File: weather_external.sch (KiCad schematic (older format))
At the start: 15 parts, among them J1 Conn_01x02_Male, J2 Conn_01x02_Male, SW1 SW_Push

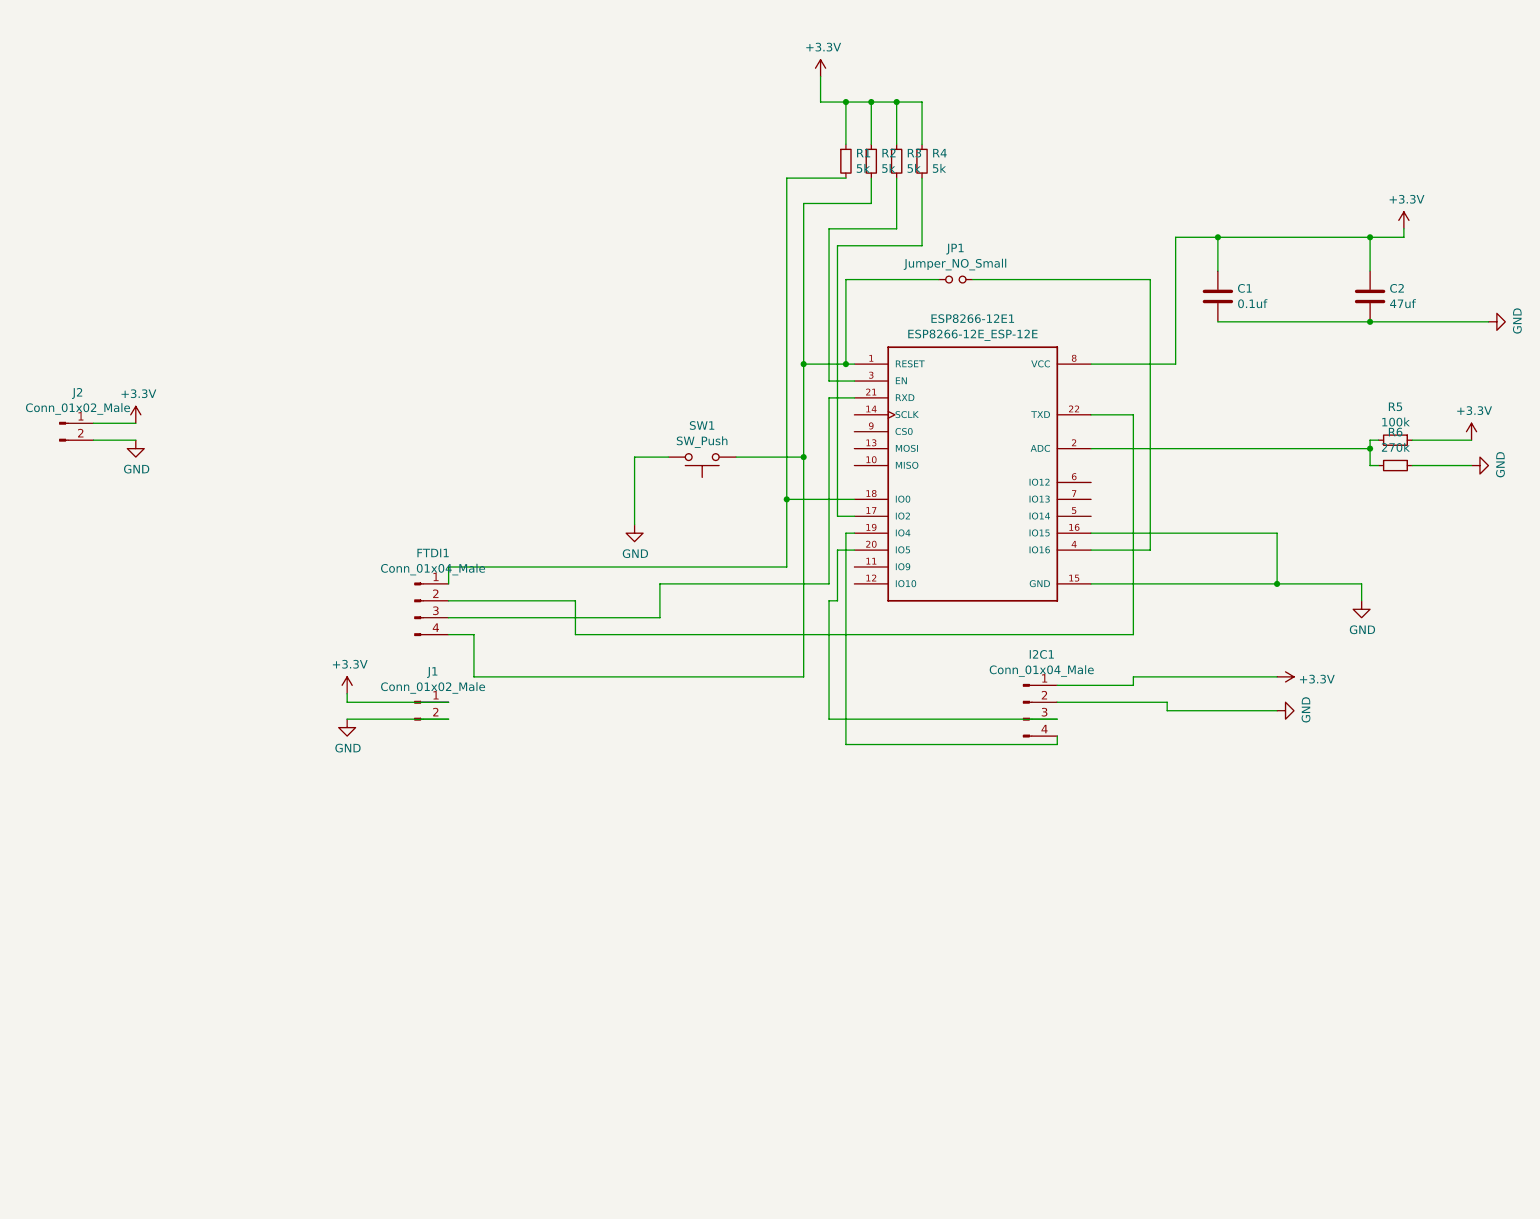
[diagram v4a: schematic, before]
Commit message: No 555 print version
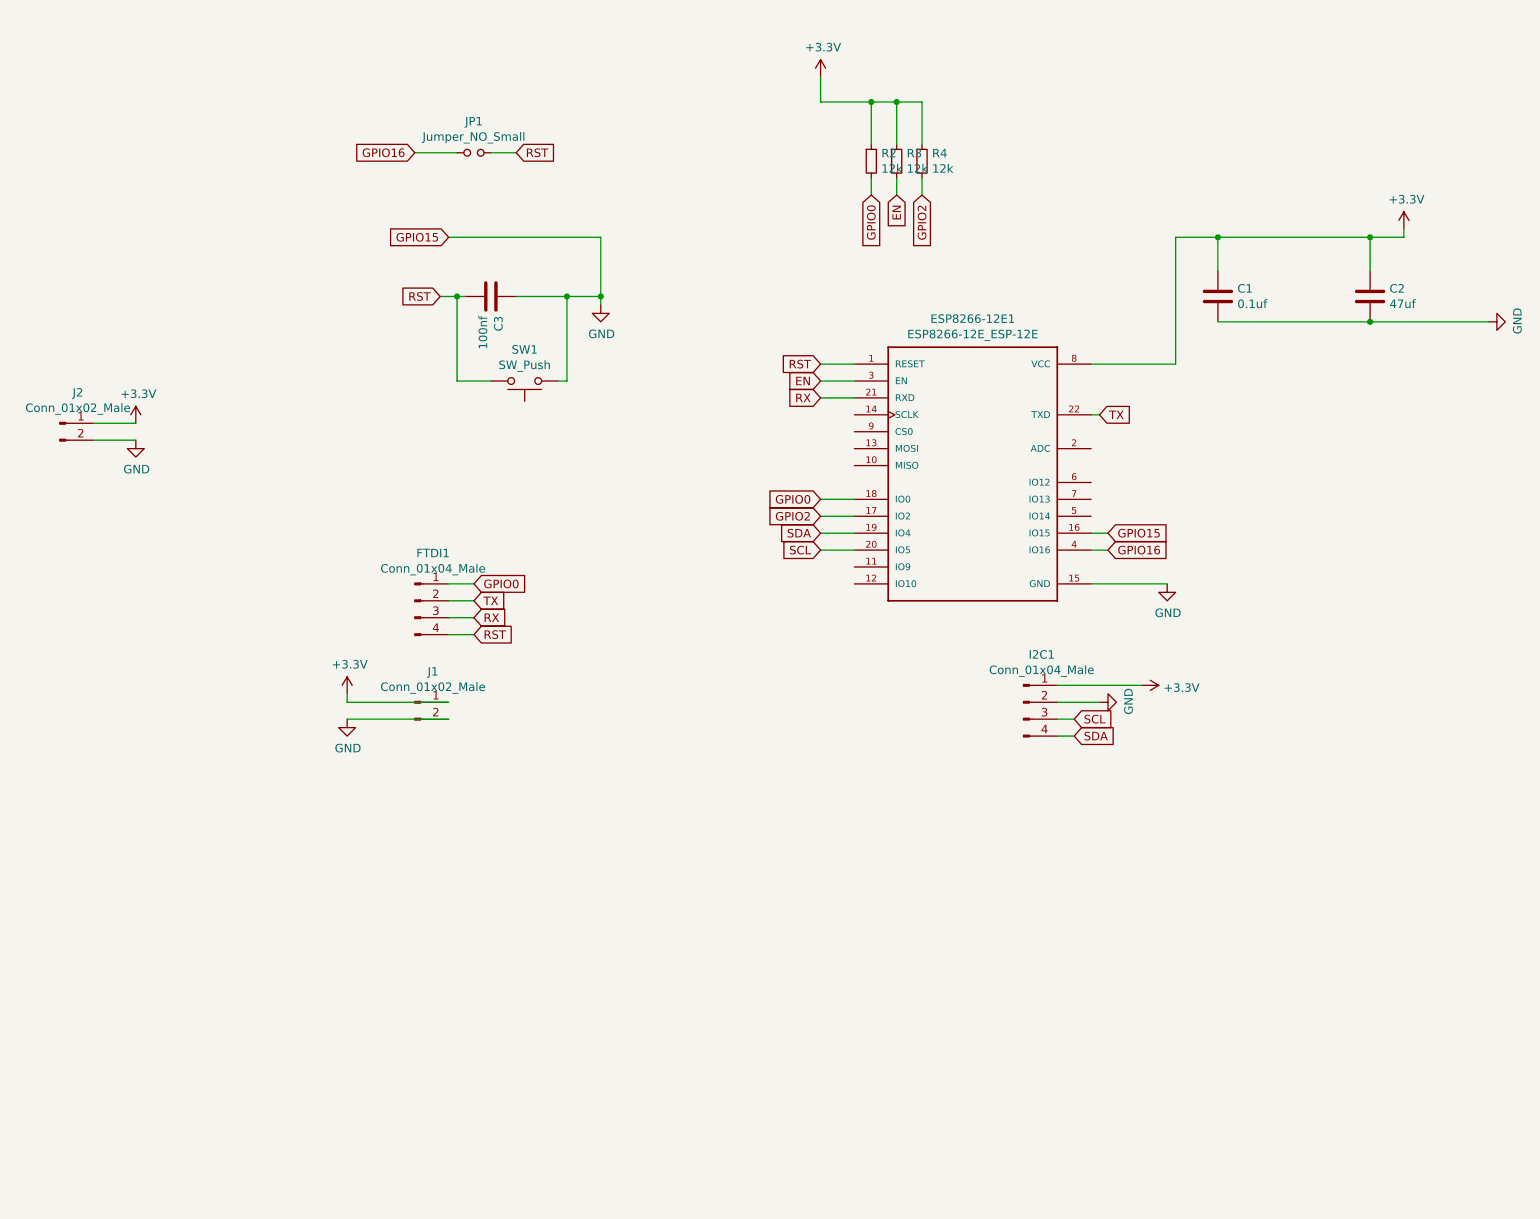
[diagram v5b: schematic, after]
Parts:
- removed R1: 5k, Resistor_THT:R_Axial_DIN0207_L6.3mm_D2.5mm_P7.62mm_Horizontal, symbol Device:R_Small
- removed R5: 100k, Resistor_THT:R_Axial_DIN0207_L6.3mm_D2.5mm_P7.62mm_Horizontal, symbol Device:R_Small
- removed R6: 270k, Resistor_THT:R_Axial_DIN0207_L6.3mm_D2.5mm_P7.62mm_Horizontal, symbol Device:R_Small
- added C3: 100nf, Capacitor_THT:C_Disc_D3.0mm_W1.6mm_P2.50mm, symbol Device:C
- R2, R3, R4: value 5k -> 12k; footprint Resistor_THT:R_Axial_DIN0207_L6.3mm_D2.5mm_P7.62mm_Horizontal -> Resistor_SMD:R_1206_3216Metric_Pad1.42x1.75mm_HandSolder
- SW1: footprint Button_Switch_THT:SW_PUSH_6mm -> Button_Switch_SMD:SW_SPST_CK_RS282G05A3
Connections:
- net GND: now also SW1.1, C3.1; no longer SW1.2
- net GPIO0: now reaches ESP8266-12E1.18 (IO0), FTDI1.1 (Pin_1)
- net GPIO0: now also R2.2
- net TX: now reaches ESP8266-12E1.22 (TXD), FTDI1.2 (Pin_2)
- net RX: now reaches ESP8266-12E1.21 (RXD), FTDI1.3 (Pin_3)
- net GPIO2: now reaches ESP8266-12E1.17 (IO2), R4.2
- net SDA: now reaches ESP8266-12E1.19 (IO4), I2C1.4 (Pin_4)
- net SCL: now reaches ESP8266-12E1.20 (IO5), I2C1.3 (Pin_3)
- net EN: now reaches ESP8266-12E1.3 (EN), R3.2
- net GPIO16: now reaches ESP8266-12E1.4 (IO16)
- net GPIO16: now also JP1.1; no longer JP1.2
- new net RST: C3.2, ESP8266-12E1.1 (RESET), FTDI1.4 (Pin_4), JP1.2, SW1.2
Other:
- moved on the sheet: JP1, SW1

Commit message: JLCPCB version 1.3
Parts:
- JP1: footprint Connector_PinHeader_2.54mm:PinHeader_1x02_P2.54mm_Vertical -> Jumper:SolderJumper-2_P1.3mm_Open_Pad1.0x1.5mm
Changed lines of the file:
@@
 Title ""
 Date ""
-Rev ""
+Rev "1.3 "
 Comp ""
 Comment1 ""
 Comment2 ""
 Comment3 ""
-Comment4 ""
+Comment4 "Jareas"
 $EndDescr
 $Comp
@@
 L power:GND #PWR0110
 U 1 1 5FB0BB1F
-P 7900 4000
-F 0 "#PWR0110" H 7900 3750 50  0001 C CNN
-F 1 "GND" H 7905 3827 50  0000 C CNN
-F 2 "" H 7900 4000 50  0001 C CNN
-F 3 "" H 7900 4000 50  0001 C CNN
-	1    7900 4000
-	1    0    0    -1
+P 7500 4000
+F 0 "#PWR0110" H 7500 3750 50  0001 C CNN
+F 1 "GND" H 7505 3827 50  0000 C CNN
+F 2 "" H 7500 4000 50  0001 C CNN
+F 3 "" H 7500 4000 50  0001 C CNN
+	1    7500 4000
+	0    -1   -1   0
 $EndComp
 $Comp
@@
 F 0 "JP1" H 3800 1635 50  0000 C CNN
 F 1 "Jumper_NO_Small" H 3800 1544 50  0000 C CNN
-F 2 "Connector_PinHeader_2.54mm:PinHeader_1x02_P2.54mm_Vertical" H 3800 1450 50  0001 C CNN
+F 2 "Jumper:SolderJumper-2_P1.3mm_Open_Pad1.0x1.5mm" H 3800 1450 50  0001 C CNN
 F 3 "~" H 3800 1450 50  0001 C CNN
 	1    3800 1450
@@
 Text GLabel 3650 1950 0    50   Input ~ 0
 GPIO15
-Wire Wire Line
-	3650 1950 4550 1950
-Wire Wire Line
-	4550 1950 4550 2300
-Connection ~ 4550 2300
 Text GLabel 7550 3700 2    50   Input ~ 0
 GPIO15
-Wire Wire Line
-	7450 4000 7900 4000
 Text GLabel 3450 1450 0    50   Input ~ 0
 GPIO16
@@
 Wire Wire Line
 	7250 4700 7500 4700
+Wire Wire Line
+	3650 1950 4350 1950
+Wire Wire Line
+	4350 1950 4350 2300
+Wire Wire Line
+	7450 4000 7500 4000
 $EndSCHEMATC

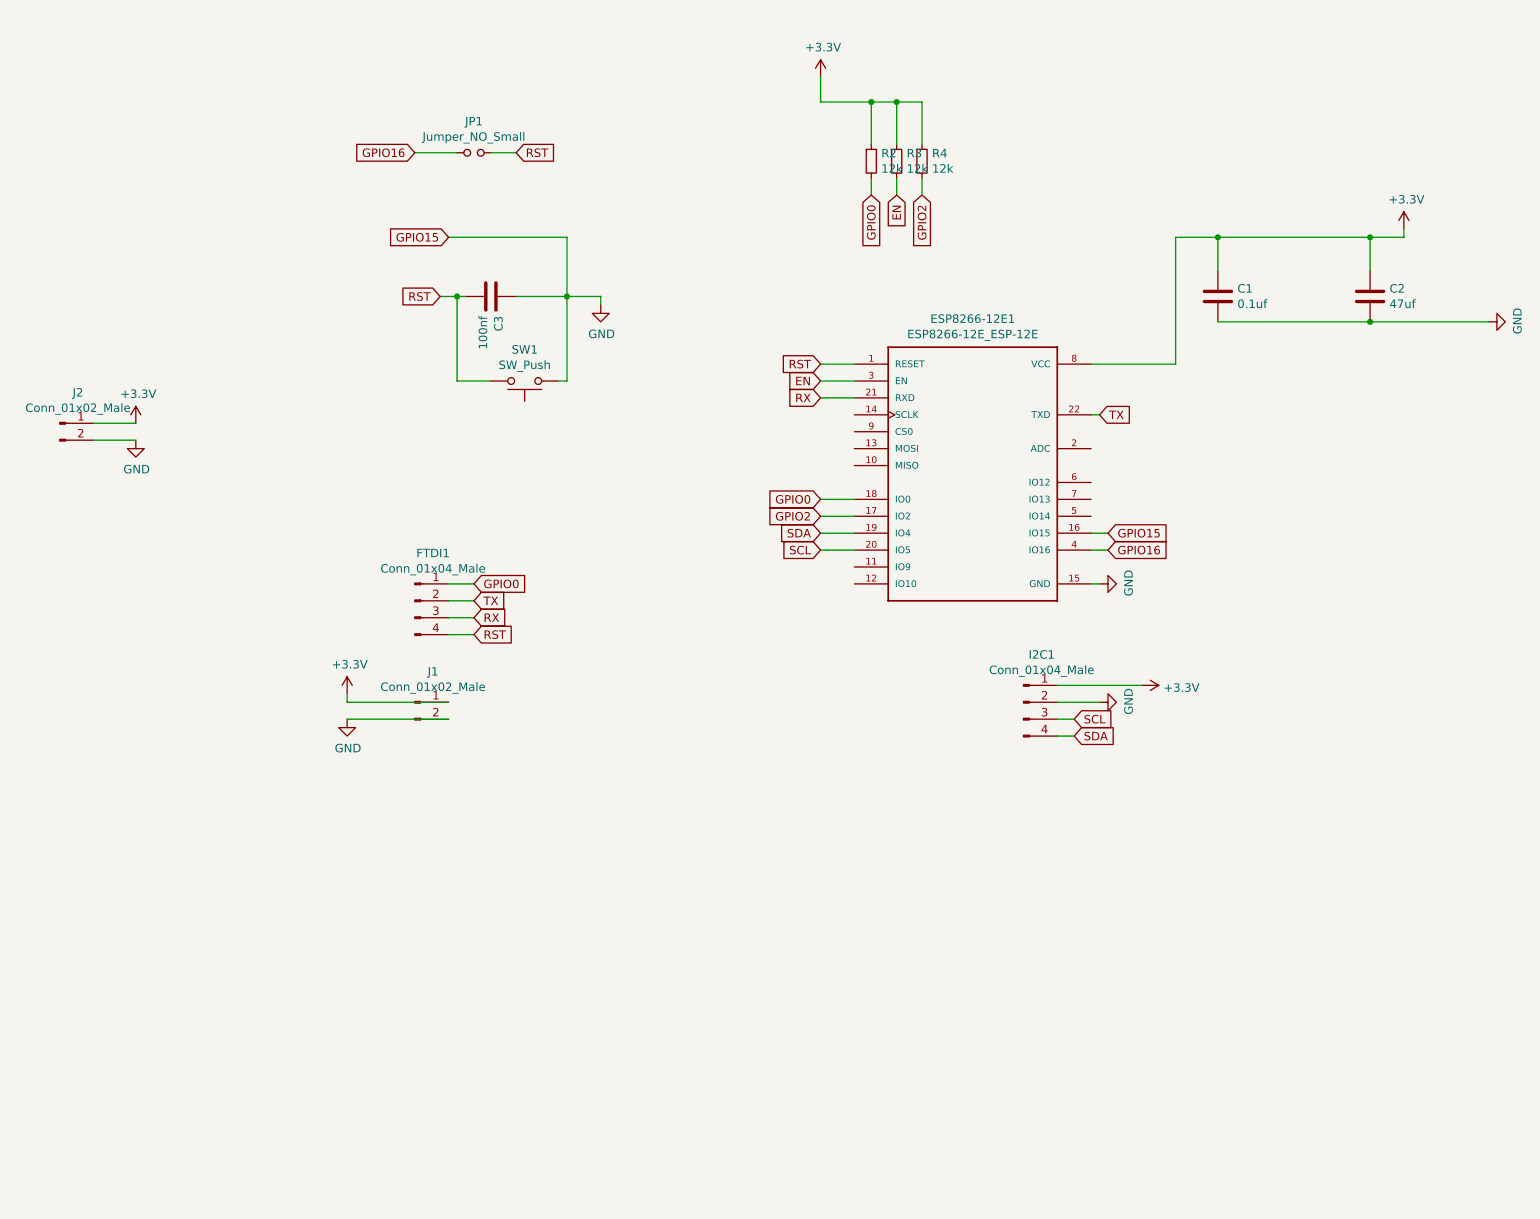
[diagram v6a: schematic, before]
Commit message: - Adding charger module TP4056 - add usb
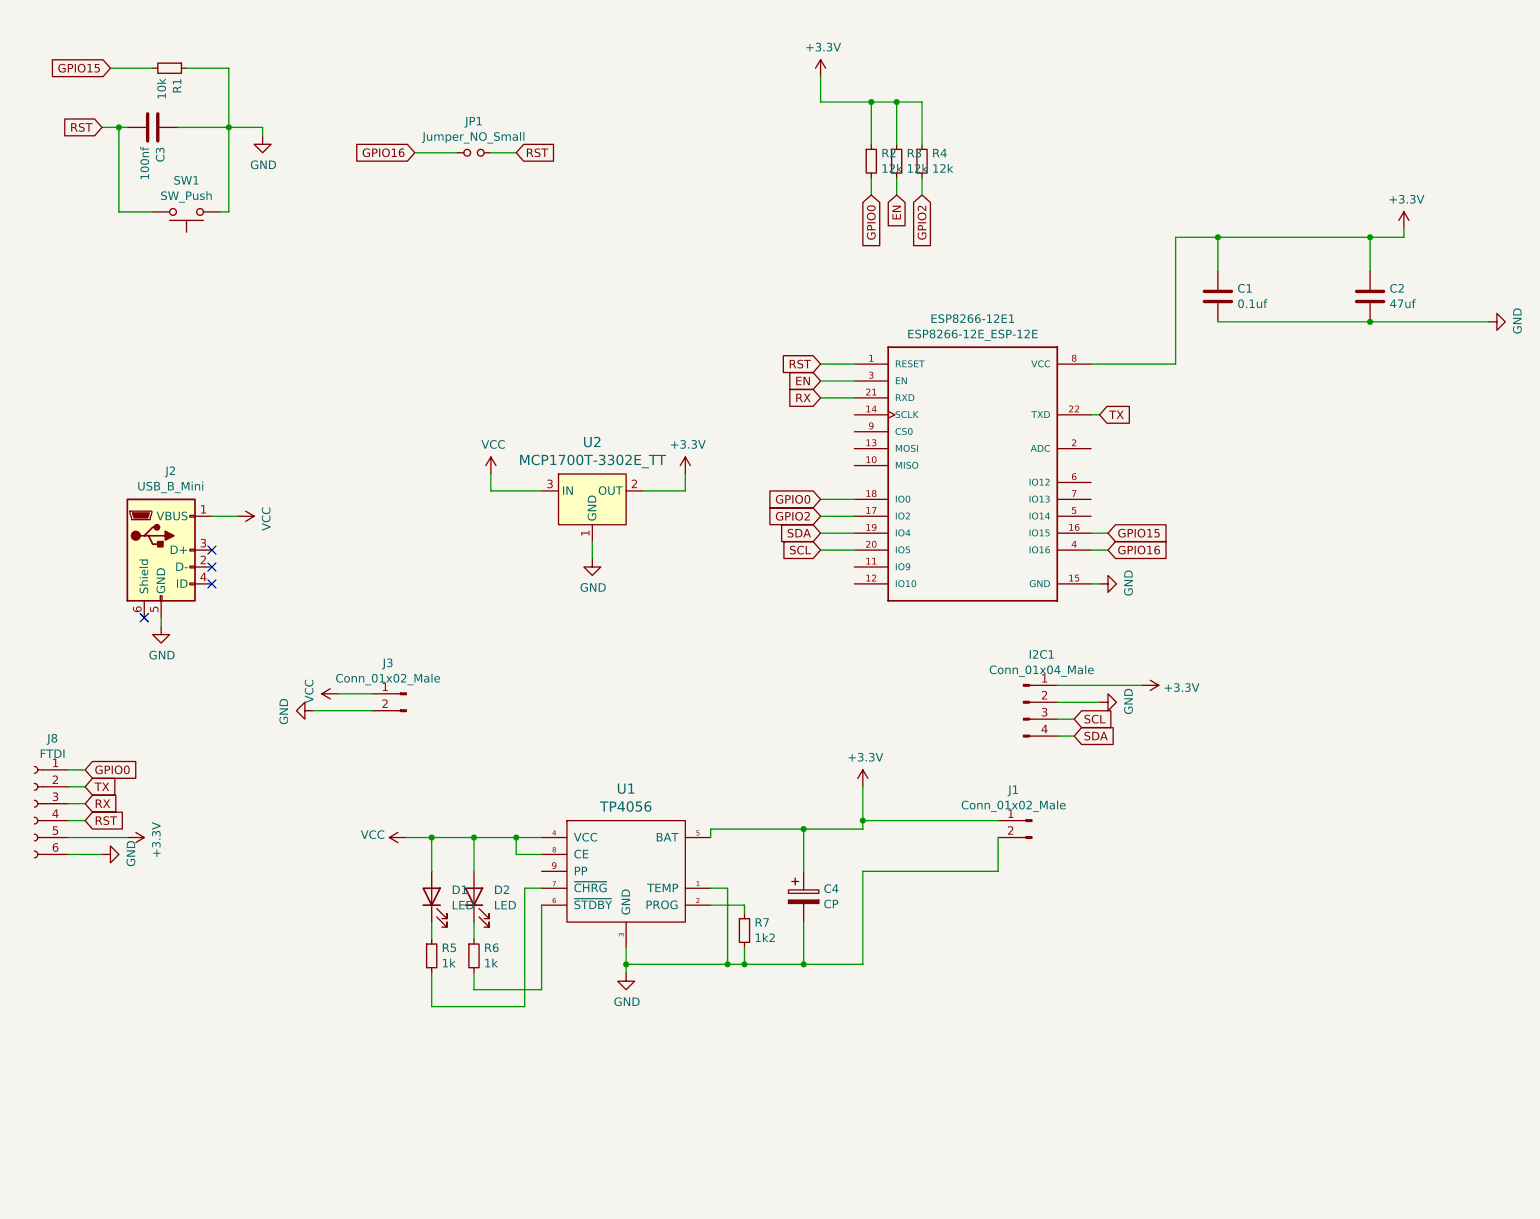
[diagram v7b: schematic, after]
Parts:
- removed FTDI1: Conn_01x04_Male, Connector_PinHeader_2.54mm:PinHeader_1x04_P2.54mm_Vertical, symbol Connector:Conn_01x04_Male
- removed J2: Conn_01x02_Male, Connector_JST:JST_PH_B2B-PH-K_1x02_P2.00mm_Vertical, symbol Connector:Conn_01x02_Male
- added C4: CP, Capacitor_THT:CP_Radial_D4.0mm_P1.50mm, symbol Device:CP
- added D1, D2: LED, LED_SMD:LED_1206_3216Metric, symbol Device:LED
- added J2: USB_B_Mini, Connector_USB:USB_Mini-B_Lumberg_2486_01_Horizontal, symbol Connector:USB_B_Mini
- added J3: Conn_01x02_Male, Connector_Wire:SolderWire-0.1sqmm_1x02_P3.6mm_D0.4mm_OD1mm, symbol Connector:Conn_01x02_Male
- added J8: FTDI, Connector_PinHeader_2.54mm:PinHeader_1x06_P2.54mm_Vertical, symbol Connector:Conn_01x06_Female
- added R1: 10k, Resistor_SMD:R_1206_3216Metric_Pad1.42x1.75mm_HandSolder, symbol Device:R_Small
- added R5, R6: 1k, Resistor_SMD:R_1206_3216Metric_Pad1.42x1.75mm_HandSolder, symbol Device:R_Small
- added R7: 1k2, Resistor_SMD:R_1206_3216Metric_Pad1.42x1.75mm_HandSolder, symbol Device:R_Small
- added U1: TP4056, Package_SO:SOP-8_3.9x4.9mm_P1.27mm, symbol tp4056:TP4056
- added U2: MCP1700T-3302E_TT, digikey-footprints:SOT-23-3, symbol dk_PMIC-Voltage-Regulators-Linear:MCP1700T-3302E_TT
- J1: footprint Connector_PinHeader_2.54mm:PinHeader_1x02_P2.54mm_Vertical -> Connector_Wire:SolderWire-0.1sqmm_1x02_P3.6mm_D0.4mm_OD1mm
- SW1: footprint Button_Switch_SMD:SW_SPST_CK_RS282G05A3 -> Button_Switch_THT:SW_PUSH_6mm_H4.3mm
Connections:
- net +3V3: now also C4.1, J8.5 (Pin_5), U1.5 (BAT), U2.2 (OUT)
- net GND: now also C4.2, J2.5 (GND), J3.2 (Pin_2), J8.6 (Pin_6), R1.1, R7.2, U1.1 (TEMP), U1.3 (GND), U2.1 (GND); no longer ESP8266-12E1.16 (IO15)
- net GPIO0: now also J8.1 (Pin_1)
- net RST: now also J8.4 (Pin_4)
- net RX: now also J8.3 (Pin_3)
- net TX: now also J8.2 (Pin_2)
- new net: R7.1, U1.2 (PROG)
- new net: R6.2, U1.6 (~STDBY)
- new net: R5.2, U1.7 (~CHRG)
- new net: D1.1 (K), R5.1
- new net: D2.1 (K), R6.1
- new net GPIO15: ESP8266-12E1.16 (IO15), R1.2
- new net VCC: D1.2 (A), D2.2 (A), J2.1 (VBUS), J3.1 (Pin_1), U1.4 (VCC), U1.8 (CE), U2.3 (IN)
- no-connect marks 0 -> 4
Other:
- moved on the sheet: C3, J1, SW1

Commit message: - Using MCP73831 to manage battery charging
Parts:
- removed U1: TP4056, Package_SO:SOP-8_3.9x4.9mm_P1.27mm, symbol tp4056:TP4056
- added C5, C6: 10nF, Capacitor_THT:CP_Radial_D4.0mm_P1.50mm, symbol Device:CP
- added C7: CP, Capacitor_THT:CP_Radial_D4.0mm_P1.50mm, symbol Device:CP
- added D3, D4: 1N4148, Diode_THT:D_T-1_P5.08mm_Horizontal, symbol Device:D
- added Q1: DMG2305UX-13, digikey-footprints:SOT-23-3, symbol dk_Transistors-FETs-MOSFETs-Single:DMG2305UX-13
- added R8: 100k, Resistor_SMD:R_1206_3216Metric_Pad1.42x1.75mm_HandSolder, symbol Device:R_Small
- added U1: MCP73831-2-OT, Package_TO_SOT_SMD:SOT-23-5, symbol Battery_Management:MCP73831-2-OT
- D1: value LED -> GREEN
- D2: value LED -> RED
- R5, R6: value 1k -> 220
- R7: value 1k2 -> 2k
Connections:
- net labels added: VBAT
- wire segments 103 -> 108
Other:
- moved on the sheet: C4, D1, D2, J1, R5, R6
